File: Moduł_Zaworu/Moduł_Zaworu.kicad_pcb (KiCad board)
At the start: 2 copper layers, 57 x 78.5 mm, 36 parts, among them J1 Screw_Terminal_01x02, J2 RJ45, J3 RJ45, J4 Screw_Terminal_01x02, J5 Screw_Terminal_01x02, J6 Screw_Terminal_01x02, J7 Screw_Terminal_01x02, J8 Screw_Terminal_01x02, U1 INA219AxD, U2 TL431D, U3 TLV172IDCK, U4 LD1117S33TR_SOT223, U5 ESP32-DEVKITC, U6 L7805

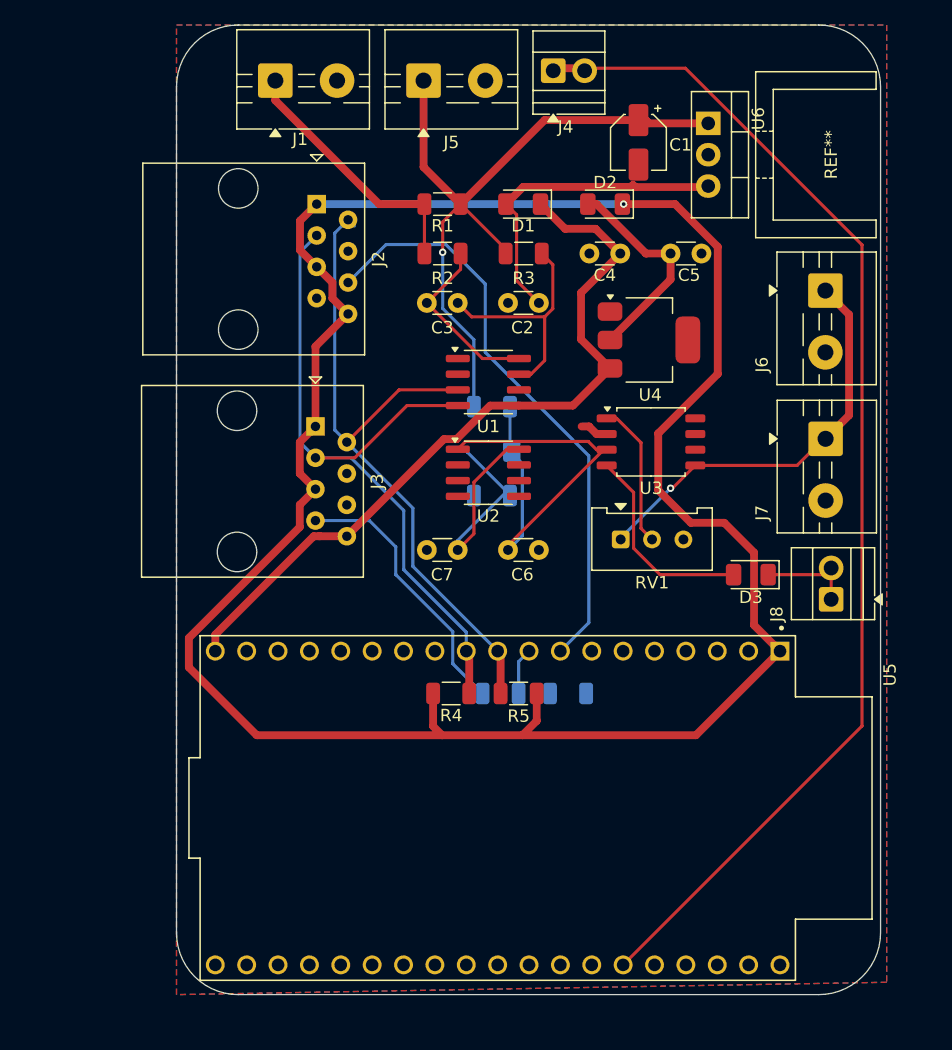
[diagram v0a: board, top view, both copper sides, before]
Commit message: Gotowy do zatwierdzenia moduł zasilaina
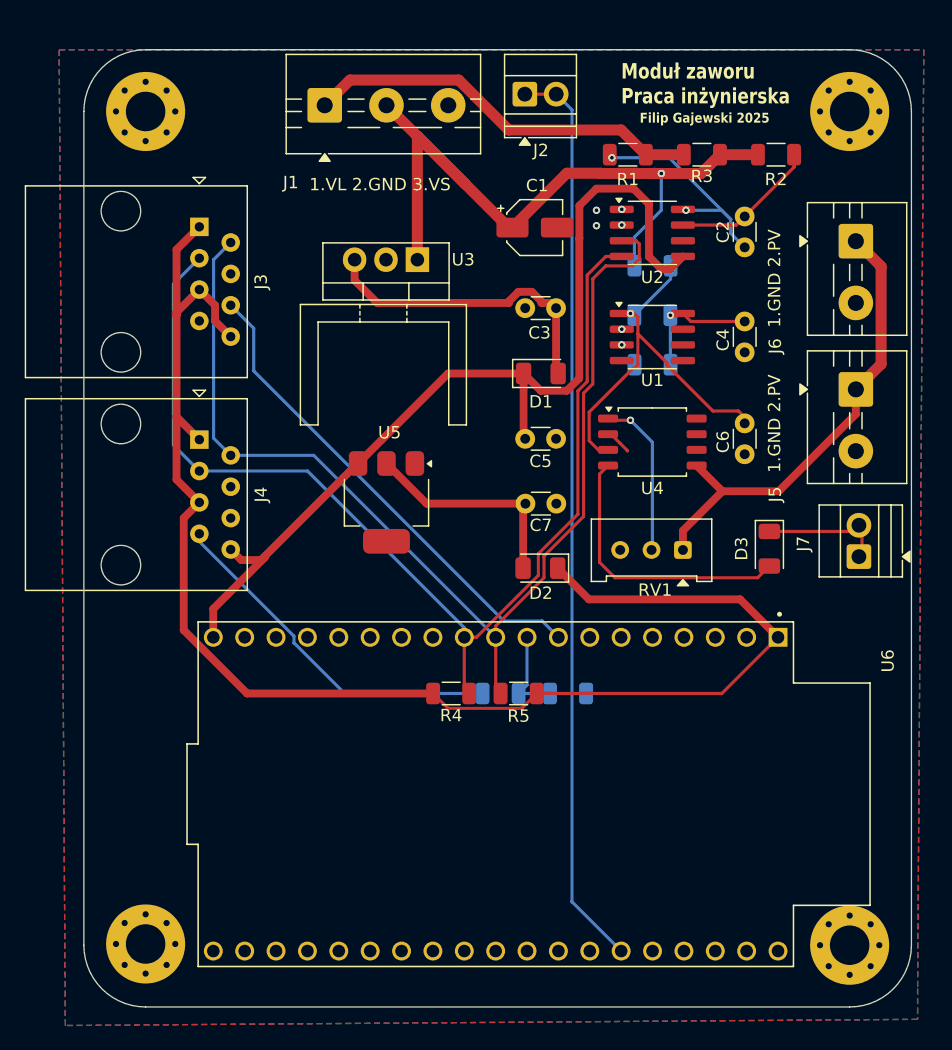
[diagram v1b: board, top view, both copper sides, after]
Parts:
- removed the J5 at (195.0, 57.0)
- removed the R7 at (200.5, 87.0)
- added R6: 10k, Resistor_SMD:R_1206_3216Metric, B.Cu at (213.5, 76.0)
- added REF**: MountingHole_3.2mm_M3_Pad_Via, MountingHole:MountingHole_3.2mm_M3_Pad_Via, F.Cu at (172.5, 59.5)
- added REF**: MountingHole_3.2mm_M3_Pad_Via, MountingHole:MountingHole_3.2mm_M3_Pad_Via, F.Cu at (229.5, 59.5)
- added REF**: MountingHole_3.2mm_M3_Pad_Via, MountingHole:MountingHole_3.2mm_M3_Pad_Via, F.Cu at (172.5, 126.9)
- added REF**: MountingHole_3.2mm_M3_Pad_Via, MountingHole:MountingHole_3.2mm_M3_Pad_Via, F.Cu at (229.5, 127.0)
- J1: value Screw_Terminal_01x02 -> Screw_Terminal_01x03; footprint TerminalBlock:TerminalBlock_MaiXu_MX126-5.0-02P_1x02_P5.00mm -> TerminalBlock:TerminalBlock_MaiXu_MX126-5.0-03P_1x03_P5.00mm
- moved REF** 32.6 mm to (191.8, 75.2), turned to 0 degrees
- moved D2 29.9 mm to (204.5, 96.5)
- moved C4 29.7 mm to (221.0, 76.5), turned to -90 degrees
- moved C2 26.1 mm to (221.0, 70.5), turned to 90 degrees
- moved U3 26.0 mm to (194.5, 71.5), turned to 180 degrees
- moved U5 25.0 mm to (192.0, 91.2), turned to -90 degrees
- moved C7 23.4 mm to (203.2, 91.2)
- moved R2 21.9 mm to (223.5, 63.0)
- moved C6 21.7 mm to (221.0, 84.8), turned to -90 degrees
- moved R3 21.4 mm to (217.5, 63.0)
- moved U2 17.9 mm to (213.5, 69.3)
- moved R8 17.3 mm to (213.5, 72.0)
- moved U1 17.2 mm to (213.5, 77.8)
- moved R1 17.0 mm to (211.5, 63.0), turned to 180 degrees
- moved C5 16.9 mm to (203.2, 86.0), turned to 0 degrees
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- renumbered C3 to C2, C2 to C3, C7 to C4, C4 to C5, C5 to C7, J4 to J2, J2 to J3, J3 to J4, J7 to J5, J8 to J7, R2 to R1, R3 to R2, R1 to R3, R8 to R7, R6 to R8, U2 to U1, U1 to U2, U6 to U3, U3 to U4, U4 to U5, U5 to U6
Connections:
- J1 pad 2: GND -> VL
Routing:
- net +3.3V: track 181.0 -> 118.3 mm, vias 1 -> 0
- net SDA: track 55.8 -> 90.1 mm
- net SCL: track 58.5 -> 88.6 mm
- net Net-(J2-Pin_1): track 97.3 -> 74.1 mm
- net +5V: track 62.0 -> 78.0 mm
- net Net-(U1-REF): track 21.7 -> 9.27 mm, vias 0 -> 1
- net VS: track 21.2 -> 32.4 mm
- net /SEN0193_WYJŚCIE: track 47.9 -> 40.0 mm
- net Net-(U2-IN-): track 19.4 -> 11.9 mm
- net Net-(J4-Pad7): track 22.2 -> 29.0 mm
- net Net-(D3-A): track 16.6 -> 22.8 mm
- net PV: track 33.6 -> 38.1 mm, vias 1 -> 0
- net Net-(U2-IN+): track 14.5 -> 18.3 mm, vias 0 -> 2
- net Vref: track 36.0 -> 32.2 mm, vias 0 -> 1
- net /Czujnik ciśnienia output: track 3.78 -> 7.37 mm
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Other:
- board size 57 x 78.5 mm -> 67 x 77.5 mm
- board text added: "1.3,3V 3.SCL 5.3,3V 7.GND 2.SDA 4.GND 6.SEN193 8.3,3V"
- board text added: "1.3,3V 3.SCL 5.3,3V 7.data 2.SDA 4.GND 6.GND 8.3,3V"
- board text added: "1.EN 2.EN"
- board text added: "1.Feedback 2.Feedback"
- board text added: "1.GND 2.PV"
- board text added: "1.VL 2.GND 3.VS"
- board text added: "BH1750FVI & SEN0193"
- board text added: "BH1750FVI & cz. ciśnienia"
- board text added: "Filip Gajewski 2025"
- board text added: "Moduł zaworu Praca inżynierska"

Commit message: Werja plików podesłana Mariuszkowi, dodane opisy i numeracja poprawna dla steronwika, w module poprawniono opis złącze ethernet
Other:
- board text added: "1.3,3V 2.SDA 3.SCL 4.GND 5.3,3V 6.GND 7.cz. c. GND 8.5V"
- board text added: "1.3,3V 2.SDA 3.SCL 4.GND 5.3,3V 6.SEN193 7.GND 8.3,3V"
- board text removed: "1.3,3V 3.SCL 5.3,3V 7.GND 2.SDA 4.GND 6.SEN193 8.3,3V"
- board text removed: "1.3,3V 3.SCL 5.3,3V 7.data 2.SDA 4.GND 6.GND 8.3,3V"
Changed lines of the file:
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@@
 		(at 200.85 114.7725 -90)
 		(property "Reference" "U6"
-			(at -10.795 -31.75 90)
+			(at 0 0 90)
 			(layer "F.SilkS")
 			(effects
@@
 		)
 	)
-	(gr_text "1.3,3V 3.SCL 5.3,3V 7.data\n2.SDA 4.GND 6.GND 8.3,3V	\n"
-		(at 184.25 82.25 90)
+	(gr_text "1.3,3V 2.SDA 3.SCL 4.GND\n5.3,3V 6.GND 7.cz. c. GND 8.5V	\n"
+		(at 184.25 81 90)
 		(layer "B.SilkS")
 		(effects
@@
 		)
 	)
-	(gr_text "1.3,3V 3.SCL 5.3,3V 7.GND\n2.SDA 4.GND 6.SEN193 8.3,3V	\n"
-		(at 184 63 90)
+	(gr_text "1.3,3V 2.SDA 3.SCL 4.GND\n5.3,3V 6.SEN193 7.GND 8.3,3V	\n"
+		(at 184 61 90)
 		(layer "B.SilkS")
 		(effects

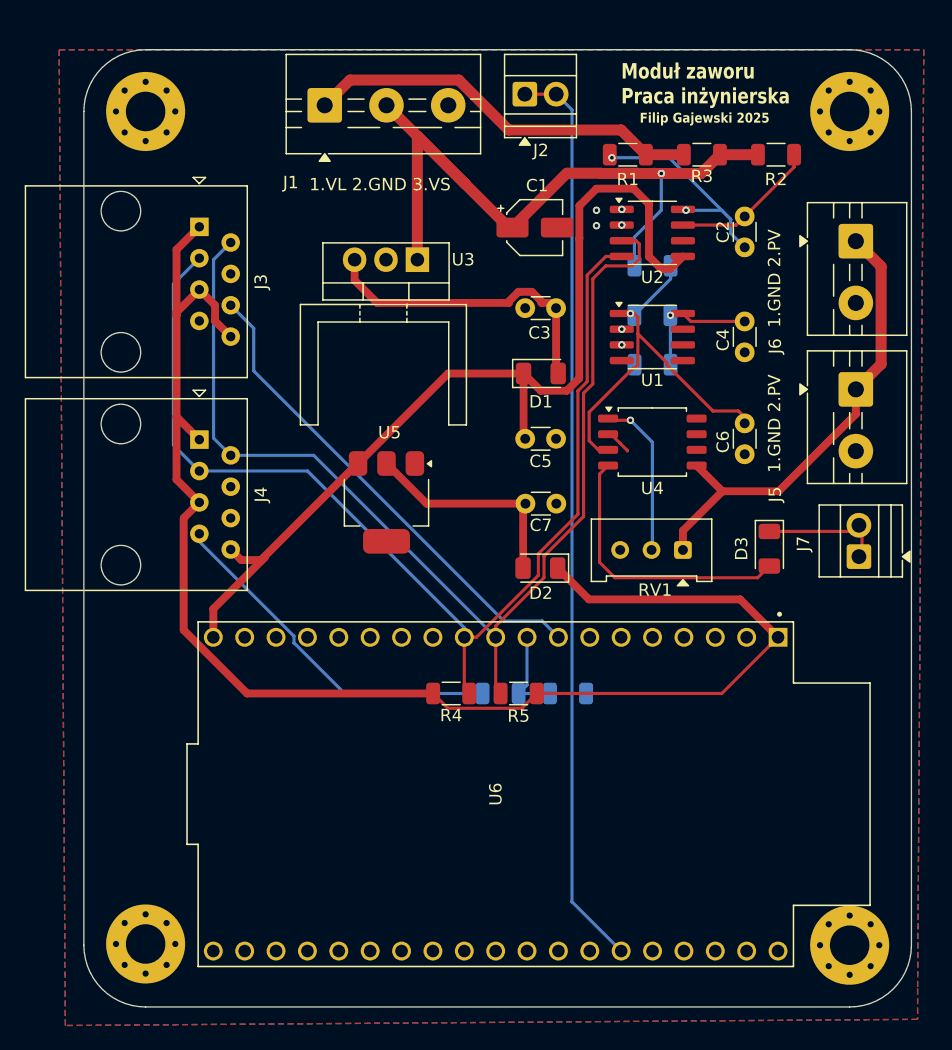
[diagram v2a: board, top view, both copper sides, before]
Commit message: Testing MQTT + apllikacja webowa+ baza danych. Dodanie zworek pozwalaąjcych na zaminę trybu przetwornicy mppt, zmiana układu zasilania zgodnie z zaleceniami Pana Mariusza.
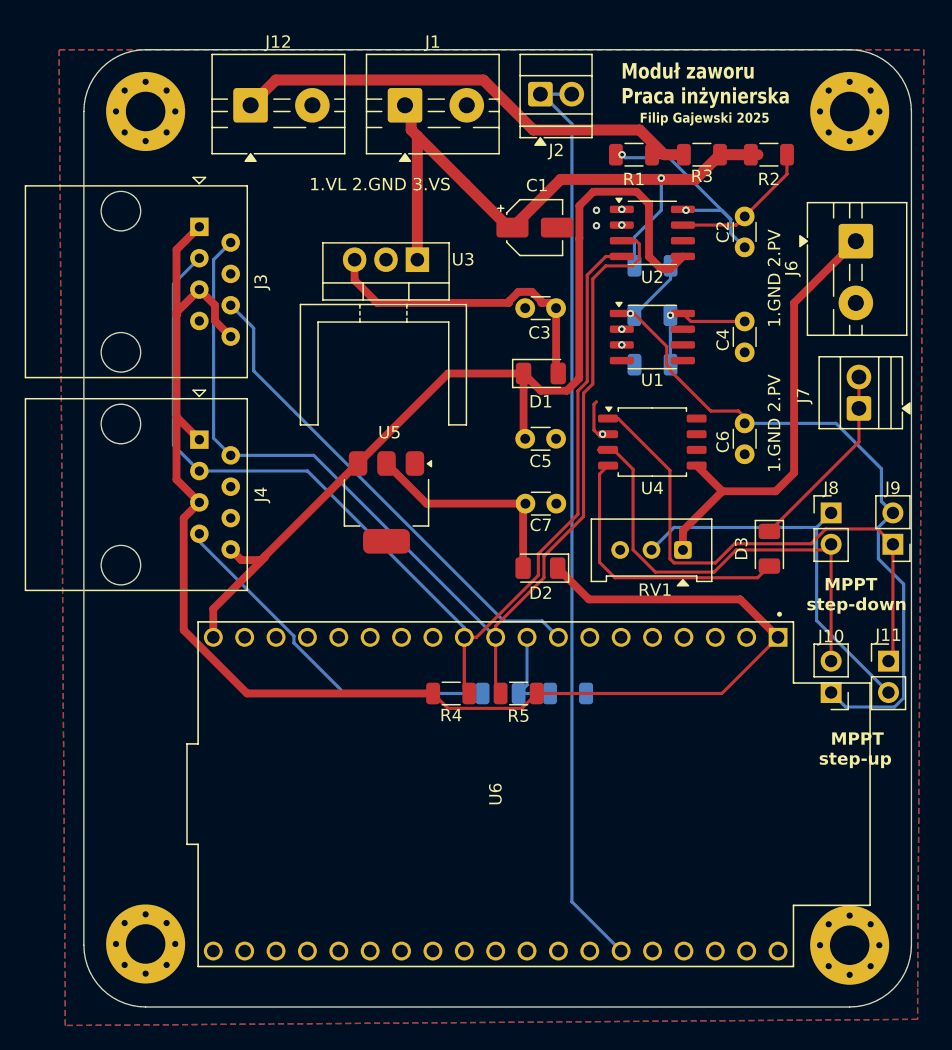
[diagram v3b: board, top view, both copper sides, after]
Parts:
- removed J5: Screw_Terminal_01x02, TerminalBlock:TerminalBlock_MaiXu_MX126-5.0-02P_1x02_P5.00mm
- added J10: Conn_01x02_Pin, Connector_PinHeader_2.54mm:PinHeader_1x02_P2.54mm_Vertical, F.Cu at (228.0, 106.5)
- added J11: Conn_01x02_Pin, Connector_PinHeader_2.54mm:PinHeader_1x02_P2.54mm_Vertical, F.Cu at (232.6, 104.0)
- added J12: Screw_Terminal_01x02, TerminalBlock:TerminalBlock_MaiXu_MX126-5.0-02P_1x02_P5.00mm, F.Cu at (181.0, 59.0)
- added J8: Conn_01x02_Pin, Connector_PinHeader_2.54mm:PinHeader_1x02_P2.54mm_Vertical, F.Cu at (228.0, 92.0)
- added J9: Conn_01x02_Pin, Connector_PinHeader_2.54mm:PinHeader_1x02_P2.54mm_Vertical, F.Cu at (233.0, 94.5)
- J1: value Screw_Terminal_01x03 -> Screw_Terminal_01x02; footprint TerminalBlock:TerminalBlock_MaiXu_MX126-5.0-03P_1x03_P5.00mm -> TerminalBlock:TerminalBlock_MaiXu_MX126-5.0-02P_1x02_P5.00mm
- moved J7 12.0 mm to (230.2, 83.5)
- moved J1 6.50 mm to (193.5, 59.0)
- moved J2 1.26 mm to (204.5, 58.1)
- moved R2 0.57 mm to (223.0, 63.0)
- moved R1 0.50 mm to (212.0, 63.0)
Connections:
- J1 pad 1: VS -> VL
- J1 pad 2: VL -> GND
- R1 pad 1: VS -> VBUS
- R3 pad 1: VS -> VBUS
- RV1 pad 2: Net-(U4-+) -> V_pot
- U4 pad 1: Net-(U4-+) -> Net-(J11-Pin_1)
- U4 pad 3: Vref -> Net-(J10-Pin_2)
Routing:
- net Net-(J11-Pin_1): track 0.00 -> 43.9 mm
- net VBUS: track 0.00 -> 38.4 mm
- net Net-(J10-Pin_2): track 0.00 -> 36.7 mm
- net VS: track 32.4 -> 0.00 mm
- net V_pot: track 0.00 -> 31.6 mm
- net Vref: track 32.2 -> 60.6 mm
- net Net-(U4-+): track 13.1 -> 0.00 mm, vias 1 -> 0
- net VL: track 60.6 -> 53.8 mm
- net Net-(D3-K): track 10.2 -> 15.5 mm
- net PV: track 38.1 -> 36.3 mm
- net GND: track 2.92 -> 4.67 mm, vias 6 -> 7
- net Net-(U2-IN-): track 11.9 -> 11.1 mm
- net Net-(U2-IN+): track 18.3 -> 17.6 mm
- net Net-(J2-Pin_1): track 74.1 -> 74.7 mm
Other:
- board text added: "1.GND 2.VBUS"
- board text added: "1.GND 2.VL"
- board text added: "MPPT step-down"
- board text added: "MPPT step-up"

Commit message: Kod websocket, kod stonka demo, kod sterownika - wszystkie taski poza bt wstepnie ogarniete
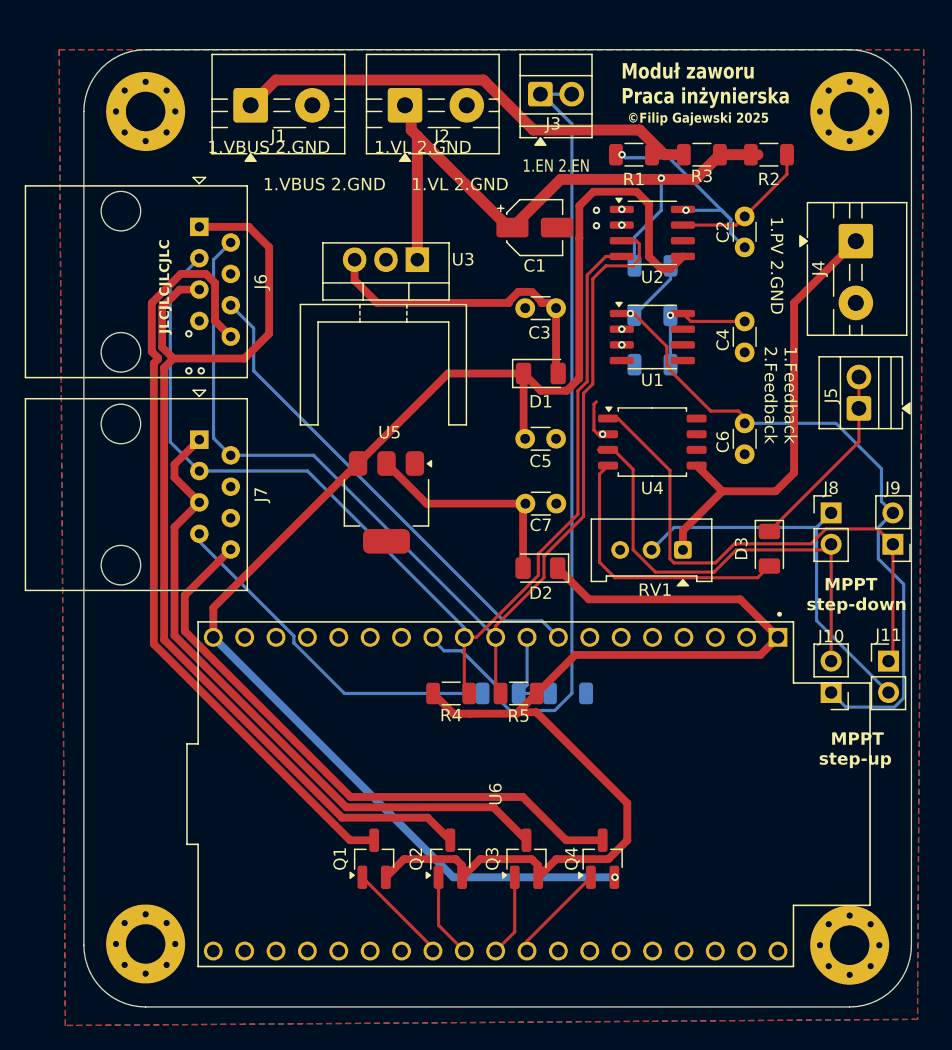
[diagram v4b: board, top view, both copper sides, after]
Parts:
- added Q1: DN2540N5-G, Package_TO_SOT_SMD:SOT-23_Handsoldering, F.Cu at (191.0, 120.0)
- added Q2: DN2540N5-G, Package_TO_SOT_SMD:SOT-23_Handsoldering, F.Cu at (197.2, 120.0)
- added Q3: DN2540N5-G, Package_TO_SOT_SMD:SOT-23_Handsoldering, F.Cu at (203.3, 120.0)
- added Q4: DN2540N5-G, Package_TO_SOT_SMD:SOT-23_Handsoldering, F.Cu at (209.5, 120.0)
- renumbered J12 to J1, J1 to J2, J2 to J3, J6 to J4, J7 to J5, J3 to J6, J4 to J7
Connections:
- J3 pad 1: Net-(J2-Pin_1) -> Net-(J3-Pin_1)
- J3 pad 2: Net-(J2-Pin_1) -> Net-(J3-Pin_1)
- J6 pad 1: +3.3V -> Net-(Q2-S)
- J6 pad 5: +3.3V -> Net-(Q2-S)
- J6 pad 8: +3.3V -> Net-(Q1-S)
- J7 pad 1: +3.3V -> Net-(Q3-S)
- J7 pad 5: +3.3V -> Net-(Q3-S)
- J7 pad 8: +5V -> Net-(Q4-S)
- U6 pad 12: unconnected-(U6-IO14-Pad12) -> Net-(J3-Pin_1)
- U6 pad 27: unconnected-(U6-IO16-Pad27) -> SEN193_POWER
- U6 pad 28: unconnected-(U6-IO17-Pad28) -> BH1750(1)_POWER
- U6 pad 29: unconnected-(U6-IO5-Pad29) -> BH1750(2)_POWER
- U6 pad 30: unconnected-(U6-IO18-Pad30) -> czujnik_cisnienia_POWER
- U6 pad 33: Net-(J2-Pin_1) -> unconnected-(U6-IO21-Pad33)
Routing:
- net Net-(Q2-S): track 0.00 -> 83.0 mm
- net Net-(J2-Pin_1): track 74.7 -> 0.00 mm
- net Net-(J3-Pin_1): track 0.00 -> 66.6 mm
- net Net-(Q1-S): track 0.00 -> 63.6 mm
- net Net-(Q3-S): track 0.00 -> 53.7 mm
- net Net-(Q4-S): track 0.00 -> 49.0 mm
- net +5V: track 77.8 -> 115.1 mm, vias 0 -> 1
- net +3.3V: track 118.3 -> 90.6 mm
- net SEN193_POWER: track 0.00 -> 8.34 mm
- net czujnik_cisnienia_POWER: track 0.00 -> 8.11 mm
- net BH1750(1)_POWER: track 0.00 -> 6.84 mm
- net BH1750(2)_POWER: track 0.00 -> 6.61 mm
- net GND: vias 7 -> 10
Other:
- board text added: "1.PV 2.GND"
- board text added: "1.VBUS 2.GND"
- board text added: "1.VL 2.GND"
- board text added: "JLCJLCJLCJLC"
- board text added: "©Filip Gajewski 2025"
- board text removed: "1.VL 2.GND 3.VS"
- board text removed: "Filip Gajewski 2025"
